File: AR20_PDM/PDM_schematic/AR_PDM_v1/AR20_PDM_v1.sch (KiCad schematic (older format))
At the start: 16 parts, among them J1 High_Curret_terminal, J2 1-776163-1, U1 ACM_2020

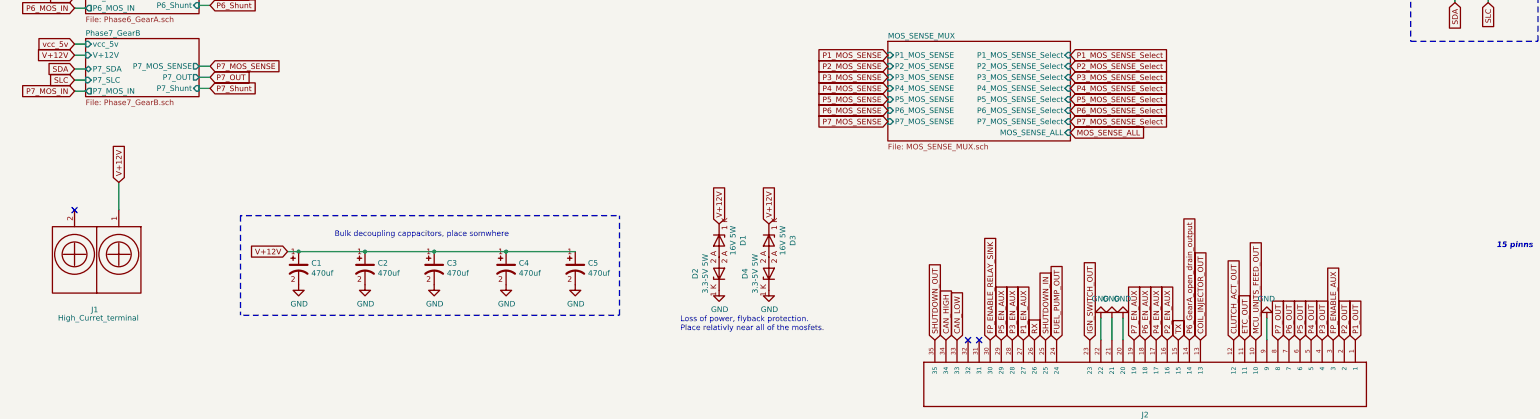
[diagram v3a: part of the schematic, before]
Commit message: Finilizing the desing, some few missing components
- Increased the size to accommodate mounting holes
- Fixed wrong p mos pin out, due to wrong schematics drawing
- Done alot of tweeeks 
- Button connector still missing.
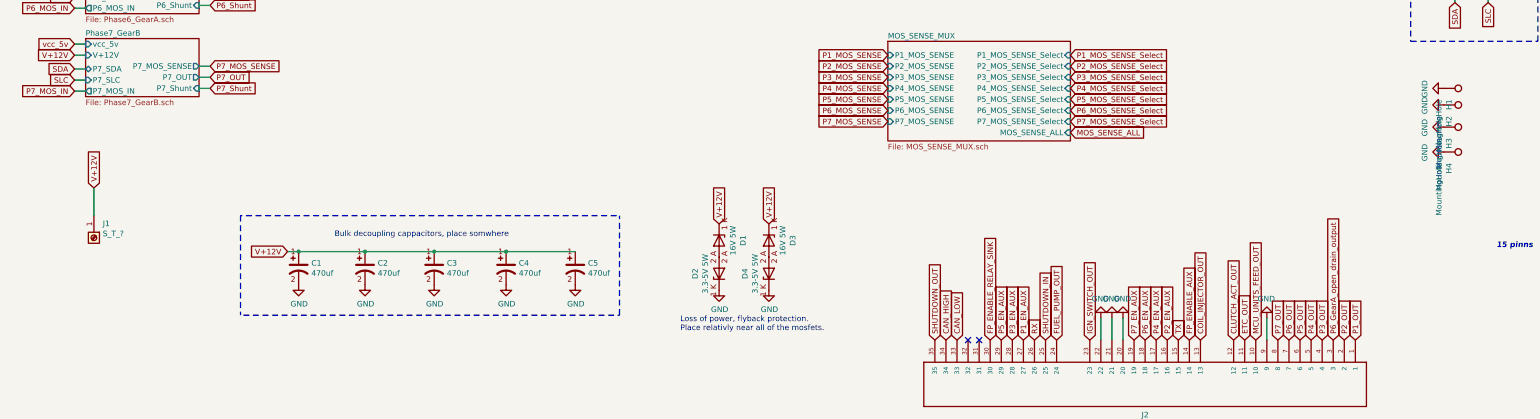
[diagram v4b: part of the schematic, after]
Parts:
- removed J1: High_Curret_terminal, Connector_Coaxial:SMA_Amphenol_132291_Vertical, symbol AR20_PDM_v1-rescue:High_Curret_terminal
- added H1, H2, H3, H4: MountingHole, MountingHole:MountingHole_3.2mm_M3_Pad_Via, symbol Connector:TestPoint
- added J1: S_T_?, AR_PDM_v1:Wurth 74655095R Screw Post, symbol Connector:Screw_Terminal_01x01
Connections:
- net FP_ENABLE_AUX: now also J2.14; no longer J2.3
- net GND: now also H1.1, H2.1, H3.1, H4.1
- net P6_GearA_open_drain_output: now also J2.3; no longer J2.14
- net V+12V: now also J1.1 (Pin_1)
- no-connect marks 12 -> 11
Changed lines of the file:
@@
 Wire Wire Line
 	8375 1800 8475 1800
-Text GLabel 1400 6450 1    50   Input ~ 0
+Text GLabel 1175 6500 1    50   Input ~ 0
 V+12V
 Text GLabel 8375 1700 0    50   Input ~ 0
@@
 vcc_5v
 Wire Wire Line
-	1400 6700 1400 6450
-$Comp
-L AR20_PDM_v1-rescue:High_Curret_terminal J1
-U 1 1 5E114D97
-P 1150 7000
-F 0 "J1" V 1750 7000 50  0000 L CNN
-F 1 "High_Curret_terminal" V 1825 6700 50  0000 L CNN
-F 2 "Connector_Coaxial:SMA_Amphenol_132291_Vertical" H 2050 6700 50  0001 C CNN
-F 3 "~" H 2050 6700 50  0001 C CNN
-	1    1150 7000
-	0    1    1    0
-$EndComp
+	1175 6750 1175 6500
 Wire Wire Line
 	2225 5400 2125 5400
@@
 Text GLabel 10575 7875 1    50   Input ~ 0
 P7_EN_AUX
-Text GLabel 12375 7875 1    50   Input ~ 0
+Text GLabel 11075 7875 1    50   Input ~ 0
 FP_ENABLE_AUX
 Text GLabel 11675 7875 1    50   Input ~ 0
@@
 Text GLabel 10975 7875 1    50   Input ~ 0
 TX
-Text GLabel 11075 7875 1    50   Input ~ 0
+Text GLabel 12375 7875 1    50   Input ~ 0
 P6_GearA_open_drain_output
 Text GLabel 9775 7875 1    50   Input ~ 0
@@
 NoConn ~ 15175 1275
 NoConn ~ 15175 1575
-NoConn ~ 1000 6700
+$Comp
+L Connector:TestPoint H1
+U 1 1 5E52DDA9
+P 13375 5600
+F 0 "H1" H 13475 5646 50  0000 L CNN
+F 1 "MountingHole" H 13475 5555 50  0000 L CNN
+F 2 "MountingHole:MountingHole_3.2mm_M3_Pad_Via" H 13375 5600 50  0001 C CNN
+F 3 "~" H 13375 5600 50  0001 C CNN
+	1    13375 5600
+	0    1    1    0
+$EndComp
+$Comp
+L Connector:TestPoint H2
+U 1 1 5E52E961
+P 13375 5750
+F 0 "H2" H 13475 5796 50  0000 L CNN
+F 1 "MountingHole" H 13475 5705 50  0000 L CNN
+F 2 "MountingHole:MountingHole_3.2mm_M3_Pad_Via" H 13375 5750 50  0001 C CNN
+F 3 "~" H 13375 5750 50  0001 C CNN
+	1    13375 5750
+	0    1    1    0
+$EndComp
+$Comp
+L Connector:TestPoint H3
+U 1 1 5E532B40
+P 13375 5950
+F 0 "H3" H 13475 5996 50  0000 L CNN
+F 1 "MountingHole" H 13475 5905 50  0000 L CNN
+F 2 "MountingHole:MountingHole_3.2mm_M3_Pad_Via" H 13375 5950 50  0001 C CNN
+F 3 "~" H 13375 5950 50  0001 C CNN
+	1    13375 5950
+	0    1    1    0
+$EndComp
+$Comp
+L Connector:Screw_Terminal_01x01 J1
+U 1 1 5E2F07B8
+P 1175 6950
+F 0 "J1" V 1047 7030 50  0000 L CNN
+F 1 "S_T_?" V 1138 7030 50  0000 L CNN
+F 2 "AR_PDM_v1:Wurth 74655095R Screw Post" H 1175 6950 50  0001 C CNN
+F 3 "~" H 1175 6950 50  0001 C CNN
+	1    1175 6950
+	0    1    1    0
+$EndComp
+$Comp
+L Connector:TestPoint H4
+U 1 1 5E536C44
+P 13375 6175
+F 0 "H4" H 13475 6221 50  0000 L CNN
+F 1 "MountingHole" H 13475 6130 50  0000 L CNN
+F 2 "MountingHole:MountingHole_3.2mm_M3_Pad_Via" H 13375 6175 50  0001 C CNN
+F 3 "~" H 13375 6175 50  0001 C CNN
+	1    13375 6175
+	0    1    1    0
+$EndComp
+$Comp
+L AR20_PDM_v1-rescue:GND-power #PWR?
+U 1 1 5E39DD75
+P 13375 5600
+AR Path="/5DA89415/5E39DD75" Ref="#PWR?"  Part="1"
+AR Path="/5DEB10A1/5E39DD75" Ref="#PWR?"  Part="1"
+AR Path="/5DEB20EA/5E39DD75" Ref="#PWR?"  Part="1"
+AR Path="/5E0E4725/5E39DD75" Ref="#PWR?"  Part="1"
+AR Path="/5E0E4A93/5E39DD75" Ref="#PWR?"  Part="1"
+AR Path="/5E0E4EB5/5E39DD75" Ref="#PWR?"  Part="1"
+AR Path="/5E0E5304/5E39DD75" Ref="#PWR?"  Part="1"
+AR Path="/5E0E594B/5E39DD75" Ref="#PWR?"  Part="1"
+AR Path="/5E0E607C/5E39DD75" Ref="#PWR?"  Part="1"
+AR Path="/5E0FB5C8/5E39DD75" Ref="#PWR?"  Part="1"
+AR Path="/5E0FBBBD/5E39DD75" Ref="#PWR?"  Part="1"
+AR Path="/5E0FC3A2/5E39DD75" Ref="#PWR?"  Part="1"
+AR Path="/5E0FCFDC/5E39DD75" Ref="#PWR?"  Part="1"
+AR Path="/5E0FDCCC/5E39DD75" Ref="#PWR?"  Part="1"
+AR Path="/5E10174B/5E39DD75" Ref="#PWR?"  Part="1"
+AR Path="/5E39DD75" Ref="#PWR?"  Part="1"
+F 0 "#PWR?" H 13375 5350 50  0001 C CNN
+F 1 "GND" H 13380 5427 50  0000 C CNN
+F 2 "" H 13375 5600 50  0001 C CNN
+F 3 "" H 13375 5600 50  0001 C CNN
+	1    13375 5600
+	0    1    1    0
+$EndComp
+$Comp
+L AR20_PDM_v1-rescue:GND-power #PWR?
+U 1 1 5E3A1F07
+P 13375 5750
+AR Path="/5DA89415/5E3A1F07" Ref="#PWR?"  Part="1"
+AR Path="/5DEB10A1/5E3A1F07" Ref="#PWR?"  Part="1"
+AR Path="/5DEB20EA/5E3A1F07" Ref="#PWR?"  Part="1"
+AR Path="/5E0E4725/5E3A1F07" Ref="#PWR?"  Part="1"
+AR Path="/5E0E4A93/5E3A1F07" Ref="#PWR?"  Part="1"
+AR Path="/5E0E4EB5/5E3A1F07" Ref="#PWR?"  Part="1"
+AR Path="/5E0E5304/5E3A1F07" Ref="#PWR?"  Part="1"
+AR Path="/5E0E594B/5E3A1F07" Ref="#PWR?"  Part="1"
+AR Path="/5E0E607C/5E3A1F07" Ref="#PWR?"  Part="1"
+AR Path="/5E0FB5C8/5E3A1F07" Ref="#PWR?"  Part="1"
+AR Path="/5E0FBBBD/5E3A1F07" Ref="#PWR?"  Part="1"
+AR Path="/5E0FC3A2/5E3A1F07" Ref="#PWR?"  Part="1"
+AR Path="/5E0FCFDC/5E3A1F07" Ref="#PWR?"  Part="1"
+AR Path="/5E0FDCCC/5E3A1F07" Ref="#PWR?"  Part="1"
+AR Path="/5E10174B/5E3A1F07" Ref="#PWR?"  Part="1"
+AR Path="/5E3A1F07" Ref="#PWR?"  Part="1"
+F 0 "#PWR?" H 13375 5500 50  0001 C CNN
+F 1 "GND" H 13380 5577 50  0000 C CNN
+F 2 "" H 13375 5750 50  0001 C CNN
+F 3 "" H 13375 5750 50  0001 C CNN
+	1    13375 5750
+	0    1    1    0
+$EndComp
+$Comp
+L AR20_PDM_v1-rescue:GND-power #PWR?
+U 1 1 5E3A60E4
+P 13375 5950
+AR Path="/5DA89415/5E3A60E4" Ref="#PWR?"  Part="1"
+AR Path="/5DEB10A1/5E3A60E4" Ref="#PWR?"  Part="1"
+AR Path="/5DEB20EA/5E3A60E4" Ref="#PWR?"  Part="1"
+AR Path="/5E0E4725/5E3A60E4" Ref="#PWR?"  Part="1"
+AR Path="/5E0E4A93/5E3A60E4" Ref="#PWR?"  Part="1"
+AR Path="/5E0E4EB5/5E3A60E4" Ref="#PWR?"  Part="1"
+AR Path="/5E0E5304/5E3A60E4" Ref="#PWR?"  Part="1"
+AR Path="/5E0E594B/5E3A60E4" Ref="#PWR?"  Part="1"
+AR Path="/5E0E607C/5E3A60E4" Ref="#PWR?"  Part="1"
+AR Path="/5E0FB5C8/5E3A60E4" Ref="#PWR?"  Part="1"
+AR Path="/5E0FBBBD/5E3A60E4" Ref="#PWR?"  Part="1"
+AR Path="/5E0FC3A2/5E3A60E4" Ref="#PWR?"  Part="1"
+AR Path="/5E0FCFDC/5E3A60E4" Ref="#PWR?"  Part="1"
+AR Path="/5E0FDCCC/5E3A60E4" Ref="#PWR?"  Part="1"
+AR Path="/5E10174B/5E3A60E4" Ref="#PWR?"  Part="1"
+AR Path="/5E3A60E4" Ref="#PWR?"  Part="1"
+F 0 "#PWR?" H 13375 5700 50  0001 C CNN
+F 1 "GND" H 13380 5777 50  0000 C CNN
+F 2 "" H 13375 5950 50  0001 C CNN
+F 3 "" H 13375 5950 50  0001 C CNN
+	1    13375 5950
+	0    1    1    0
+$EndComp
+$Comp
+L AR20_PDM_v1-rescue:GND-power #PWR?
+U 1 1 5E3AA1FC
+P 13375 6175
+AR Path="/5DA89415/5E3AA1FC" Ref="#PWR?"  Part="1"
+AR Path="/5DEB10A1/5E3AA1FC" Ref="#PWR?"  Part="1"
+AR Path="/5DEB20EA/5E3AA1FC" Ref="#PWR?"  Part="1"
+AR Path="/5E0E4725/5E3AA1FC" Ref="#PWR?"  Part="1"
+AR Path="/5E0E4A93/5E3AA1FC" Ref="#PWR?"  Part="1"
+AR Path="/5E0E4EB5/5E3AA1FC" Ref="#PWR?"  Part="1"
+AR Path="/5E0E5304/5E3AA1FC" Ref="#PWR?"  Part="1"
+AR Path="/5E0E594B/5E3AA1FC" Ref="#PWR?"  Part="1"
+AR Path="/5E0E607C/5E3AA1FC" Ref="#PWR?"  Part="1"
+AR Path="/5E0FB5C8/5E3AA1FC" Ref="#PWR?"  Part="1"
+AR Path="/5E0FBBBD/5E3AA1FC" Ref="#PWR?"  Part="1"
+AR Path="/5E0FC3A2/5E3AA1FC" Ref="#PWR?"  Part="1"
+AR Path="/5E0FCFDC/5E3AA1FC" Ref="#PWR?"  Part="1"
+AR Path="/5E0FDCCC/5E3AA1FC" Ref="#PWR?"  Part="1"
+AR Path="/5E10174B/5E3AA1FC" Ref="#PWR?"  Part="1"
+AR Path="/5E3AA1FC" Ref="#PWR?"  Part="1"
+F 0 "#PWR?" H 13375 5925 50  0001 C CNN
+F 1 "GND" H 13380 6002 50  0000 C CNN
+F 2 "" H 13375 6175 50  0001 C CNN
+F 3 "" H 13375 6175 50  0001 C CNN
+	1    13375 6175
+	0    1    1    0
+$EndComp
 $EndSCHEMATC

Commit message: Alpha version DONE! - Gerber files generated
- Tweeked
- checked and re cheked
- added all missing components
- Created a really nice silkscreen
- Ready To Test
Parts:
- U1: footprint AR_PDM_v1:ACM_2020_Footprint -> AR_PDM_v1:ACM_2020_Footprint_wo_silk
- renumbered C_sense1 to C6, H3 to H1, H1 to H3, R_sense1 to R1, R10K1 to R2, R10K2 to R3
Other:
- moved on the sheet: H1, H2, H3, H4, J1

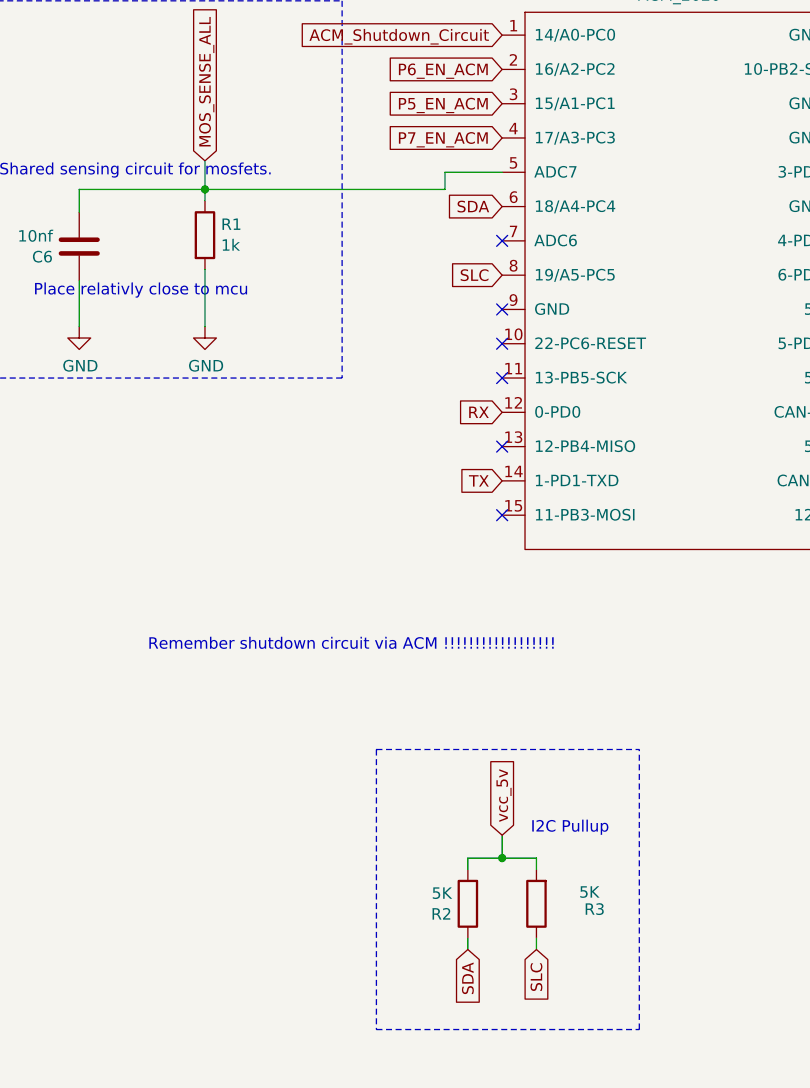
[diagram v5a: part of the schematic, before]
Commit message: Fixed wrong resistors, mos sense. Gerber files updated
- removed all R_is_protection resistors on each mosfet line
- added one R_is_protection resistors to mos_sense_all
ps, mux N-fets, does not need overvoltage protection. 60 volt tolerant.
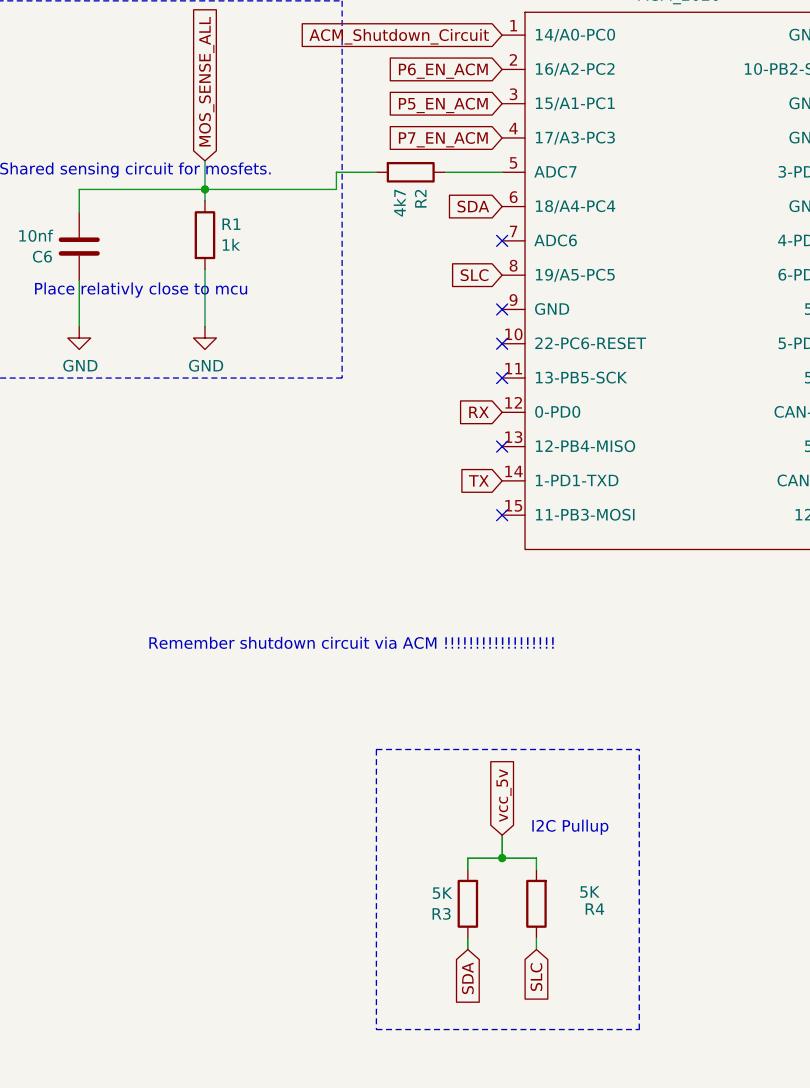
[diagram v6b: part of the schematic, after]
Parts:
- added R2: 4k7, Resistor_SMD:R_0603_1608Metric, symbol AR20_PDM_v1-rescue:R-Device
- renumbered R2 to R3, R3 to R4
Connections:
- net MOS_SENSE_ALL: now also R2.2; no longer U1.5 (ADC7)
- new net: R2.1, U1.5 (ADC7)
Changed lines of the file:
@@
 P 13475 4625
 AR Path="/5DA89415/5DAD3BC1" Ref="R?"  Part="1"
-AR Path="/5DAD3BC1" Ref="R2"  Part="1"
-F 0 "R2" H 13545 4671 50  0000 L CNN
+AR Path="/5DAD3BC1" Ref="R3"  Part="1"
+F 0 "R3" H 13545 4671 50  0000 L CNN
 F 1 "5K" H 13545 4580 50  0000 L CNN
 F 2 "Resistor_SMD:R_0603_1608Metric" V 13405 4625 50  0001 C CNN
@@
 P 13775 4625
 AR Path="/5DA89415/5E228553" Ref="R?"  Part="1"
-AR Path="/5E228553" Ref="R3"  Part="1"
-F 0 "R3" H 13475 4650 50  0000 L CNN
+AR Path="/5E228553" Ref="R4"  Part="1"
+F 0 "R4" H 13475 4650 50  0000 L CNN
 F 1 "5K" H 13500 4575 50  0000 L CNN
 F 2 "Resistor_SMD:R_0603_1608Metric" V 13705 4625 50  0001 C CNN
@@
 	2225 1075 2125 1075
 Wire Wire Line
-	12325 2100 12325 1850
-$Comp
-L AR20_PDM_v1-rescue:R-Device R?
-U 1 1 5E344AEE
-P 12325 1700
-AR Path="/5DA89415/5E344AEE" Ref="R?"  Part="1"
-AR Path="/5DEB10A1/5E344AEE" Ref="R?"  Part="1"
-AR Path="/5DEB20EA/5E344AEE" Ref="R?"  Part="1"
-AR Path="/5E0E4725/5E344AEE" Ref="R?"  Part="1"
-AR Path="/5E0E4A93/5E344AEE" Ref="R?"  Part="1"
-AR Path="/5E0E4EB5/5E344AEE" Ref="R?"  Part="1"
-AR Path="/5E0E5304/5E344AEE" Ref="R?"  Part="1"
-AR Path="/5E0E594B/5E344AEE" Ref="R?"  Part="1"
-AR Path="/5E0E607C/5E344AEE" Ref="R?"  Part="1"
-AR Path="/5E0FB5C8/5E344AEE" Ref="R?"  Part="1"
-AR Path="/5E0FBBBD/5E344AEE" Ref="R?"  Part="1"
-AR Path="/5E0FC3A2/5E344AEE" Ref="R?"  Part="1"
-AR Path="/5E0FCFDC/5E344AEE" Ref="R?"  Part="1"
-AR Path="/5E0FDCCC/5E344AEE" Ref="R?"  Part="1"
-AR Path="/5E10174B/5E344AEE" Ref="R?"  Part="1"
-AR Path="/5E344AEE" Ref="R1"  Part="1"
-F 0 "R1" H 12395 1746 50  0000 L CNN
-F 1 "1k" H 12395 1655 50  0000 L CNN
-F 2 "Resistor_SMD:R_0603_1608Metric" V 12255 1700 50  0001 C CNN
-F 3 "~" H 12325 1700 50  0001 C CNN
-	1    12325 1700
-	1    0    0    -1
-$EndComp
-$Comp
-L AR20_PDM_v1-rescue:GND-power #PWR?
-U 1 1 5E344AF4
-P 12325 2100
-AR Path="/5DA89415/5E344AF4" Ref="#PWR?"  Part="1"
-AR Path="/5DEB10A1/5E344AF4" Ref="#PWR?"  Part="1"
-AR Path="/5DEB20EA/5E344AF4" Ref="#PWR?"  Part="1"
-AR Path="/5E0E4725/5E344AF4" Ref="#PWR?"  Part="1"
-AR Path="/5E0E4A93/5E344AF4" Ref="#PWR?"  Part="1"
-AR Path="/5E0E4EB5/5E344AF4" Ref="#PWR?"  Part="1"
-AR Path="/5E0E5304/5E344AF4" Ref="#PWR?"  Part="1"
-AR Path="/5E0E594B/5E344AF4" Ref="#PWR?"  Part="1"
-AR Path="/5E0E607C/5E344AF4" Ref="#PWR?"  Part="1"
-AR Path="/5E0FB5C8/5E344AF4" Ref="#PWR?"  Part="1"
-AR Path="/5E0FBBBD/5E344AF4" Ref="#PWR?"  Part="1"
-AR Path="/5E0FC3A2/5E344AF4" Ref="#PWR?"  Part="1"
-AR Path="/5E0FCFDC/5E344AF4" Ref="#PWR?"  Part="1"
-AR Path="/5E0FDCCC/5E344AF4" Ref="#PWR?"  Part="1"
-AR Path="/5E10174B/5E344AF4" Ref="#PWR?"  Part="1"
-AR Path="/5E344AF4" Ref="#PWR013"  Part="1"
-F 0 "#PWR013" H 12325 1850 50  0001 C CNN
-F 1 "GND" H 12330 1927 50  0000 C CNN
-F 2 "" H 12325 2100 50  0001 C CNN
-F 3 "" H 12325 2100 50  0001 C CNN
-	1    12325 2100
-	1    0    0    -1
-$EndComp
-Wire Wire Line
 	12325 1375 12325 1500
 Connection ~ 12325 1500
@@
 	1    0    0    -1
 $EndComp
-Wire Wire Line
-	12325 1500 12325 1550
 Text GLabel 12325 1375 1    50   Input ~ 0
 MOS_SENSE_ALL
 Text GLabel 13625 975  0    50   Input ~ 0
 P6_EN_ACM
-Text Notes 11575 1975 0    50   ~ 0
-Place relativly close to mcu
 Text Notes 11425 1450 0    50   ~ 0
 Shared sensing circuit for mosfets.
@@
 	11250 675  12925 675
 Wire Wire Line
-	13375 1500 13375 1425
-Wire Wire Line
 	13375 1425 13625 1425
-Wire Wire Line
-	12325 1500 13375 1500
 Text GLabel 8225 4025 0    50   Input ~ 0
 FP_Alert
@@
 	0    1    1    0
 $EndComp
+Text Notes 11575 1975 0    50   ~ 0
+Place relativly close to mcu
+Wire Wire Line
+	12325 1500 12325 1550
+$Comp
+L AR20_PDM_v1-rescue:R-Device R?
+U 1 1 5E344AEE
+P 12325 1700
+AR Path="/5DA89415/5E344AEE" Ref="R?"  Part="1"
+AR Path="/5DEB10A1/5E344AEE" Ref="R?"  Part="1"
+AR Path="/5DEB20EA/5E344AEE" Ref="R?"  Part="1"
+AR Path="/5E0E4725/5E344AEE" Ref="R?"  Part="1"
+AR Path="/5E0E4A93/5E344AEE" Ref="R?"  Part="1"
+AR Path="/5E0E4EB5/5E344AEE" Ref="R?"  Part="1"
+AR Path="/5E0E5304/5E344AEE" Ref="R?"  Part="1"
+AR Path="/5E0E594B/5E344AEE" Ref="R?"  Part="1"
+AR Path="/5E0E607C/5E344AEE" Ref="R?"  Part="1"
+AR Path="/5E0FB5C8/5E344AEE" Ref="R?"  Part="1"
+AR Path="/5E0FBBBD/5E344AEE" Ref="R?"  Part="1"
+AR Path="/5E0FC3A2/5E344AEE" Ref="R?"  Part="1"
+AR Path="/5E0FCFDC/5E344AEE" Ref="R?"  Part="1"
+AR Path="/5E0FDCCC/5E344AEE" Ref="R?"  Part="1"
+AR Path="/5E10174B/5E344AEE" Ref="R?"  Part="1"
+AR Path="/5E344AEE" Ref="R1"  Part="1"
+F 0 "R1" H 12395 1746 50  0000 L CNN
+F 1 "1k" H 12395 1655 50  0000 L CNN
+F 2 "Resistor_SMD:R_0603_1608Metric" V 12255 1700 50  0001 C CNN
+F 3 "~" H 12325 1700 50  0001 C CNN
+	1    12325 1700
+	1    0    0    -1
+$EndComp
+Wire Wire Line
+	12325 2100 12325 1850
+$Comp
+L AR20_PDM_v1-rescue:GND-power #PWR?
+U 1 1 5E344AF4
+P 12325 2100
+AR Path="/5DA89415/5E344AF4" Ref="#PWR?"  Part="1"
+AR Path="/5DEB10A1/5E344AF4" Ref="#PWR?"  Part="1"
+AR Path="/5DEB20EA/5E344AF4" Ref="#PWR?"  Part="1"
+AR Path="/5E0E4725/5E344AF4" Ref="#PWR?"  Part="1"
+AR Path="/5E0E4A93/5E344AF4" Ref="#PWR?"  Part="1"
+AR Path="/5E0E4EB5/5E344AF4" Ref="#PWR?"  Part="1"
+AR Path="/5E0E5304/5E344AF4" Ref="#PWR?"  Part="1"
+AR Path="/5E0E594B/5E344AF4" Ref="#PWR?"  Part="1"
+AR Path="/5E0E607C/5E344AF4" Ref="#PWR?"  Part="1"
+AR Path="/5E0FB5C8/5E344AF4" Ref="#PWR?"  Part="1"
+AR Path="/5E0FBBBD/5E344AF4" Ref="#PWR?"  Part="1"
+AR Path="/5E0FC3A2/5E344AF4" Ref="#PWR?"  Part="1"
+AR Path="/5E0FCFDC/5E344AF4" Ref="#PWR?"  Part="1"
+AR Path="/5E0FDCCC/5E344AF4" Ref="#PWR?"  Part="1"
+AR Path="/5E10174B/5E344AF4" Ref="#PWR?"  Part="1"
+AR Path="/5E344AF4" Ref="#PWR013"  Part="1"
+F 0 "#PWR013" H 12325 1850 50  0001 C CNN
+F 1 "GND" H 12330 1927 50  0000 C CNN
+F 2 "" H 12325 2100 50  0001 C CNN
+F 3 "" H 12325 2100 50  0001 C CNN
+	1    12325 2100
+	1    0    0    -1
+$EndComp
+Wire Wire Line
+	12900 1500 12900 1425
+Wire Wire Line
+	12325 1500 12900 1500
+$Comp
+L AR20_PDM_v1-rescue:R-Device R?
+U 1 1 5E3839E0
+P 13225 1425
+AR Path="/5DA89415/5E3839E0" Ref="R?"  Part="1"
+AR Path="/5DEB10A1/5E3839E0" Ref="R?"  Part="1"
+AR Path="/5DEB20EA/5E3839E0" Ref="R?"  Part="1"
+AR Path="/5E0E4725/5E3839E0" Ref="R?"  Part="1"
+AR Path="/5E0E4A93/5E3839E0" Ref="R?"  Part="1"
+AR Path="/5E0E4EB5/5E3839E0" Ref="R?"  Part="1"
+AR Path="/5E0E5304/5E3839E0" Ref="R?"  Part="1"
+AR Path="/5E0E594B/5E3839E0" Ref="R?"  Part="1"
+AR Path="/5E0E607C/5E3839E0" Ref="R?"  Part="1"
+AR Path="/5E0FB5C8/5E3839E0" Ref="R?"  Part="1"
+AR Path="/5E0FBBBD/5E3839E0" Ref="R?"  Part="1"
+AR Path="/5E0FC3A2/5E3839E0" Ref="R?"  Part="1"
+AR Path="/5E0FCFDC/5E3839E0" Ref="R?"  Part="1"
+AR Path="/5E0FDCCC/5E3839E0" Ref="R?"  Part="1"
+AR Path="/5E10174B/5E3839E0" Ref="R?"  Part="1"
+AR Path="/5E3839E0" Ref="R2"  Part="1"
+F 0 "R2" H 13295 1471 50  0000 L CNN
+F 1 "4k7" H 13295 1380 50  0000 L CNN
+F 2 "Resistor_SMD:R_0603_1608Metric" V 13155 1425 50  0001 C CNN
+F 3 "~" H 13225 1425 50  0001 C CNN
+	1    13225 1425
+	0    1    1    0
+$EndComp
+Wire Wire Line
+	12900 1425 13075 1425
 $EndSCHEMATC
